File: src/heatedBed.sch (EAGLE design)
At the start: 10 parts

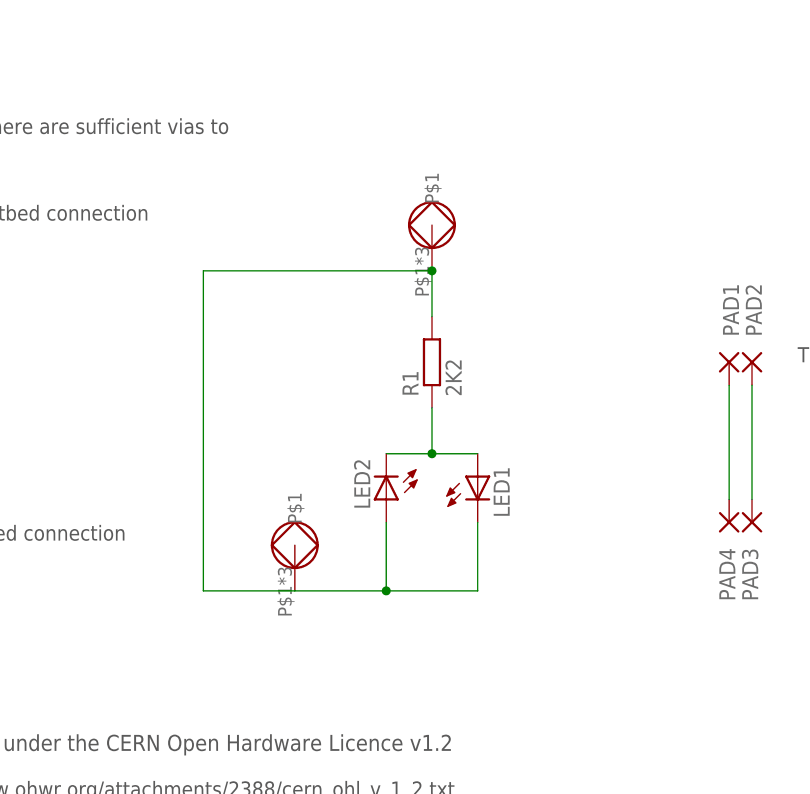
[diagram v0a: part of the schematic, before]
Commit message: Updated PCB for bottom mount LEDs
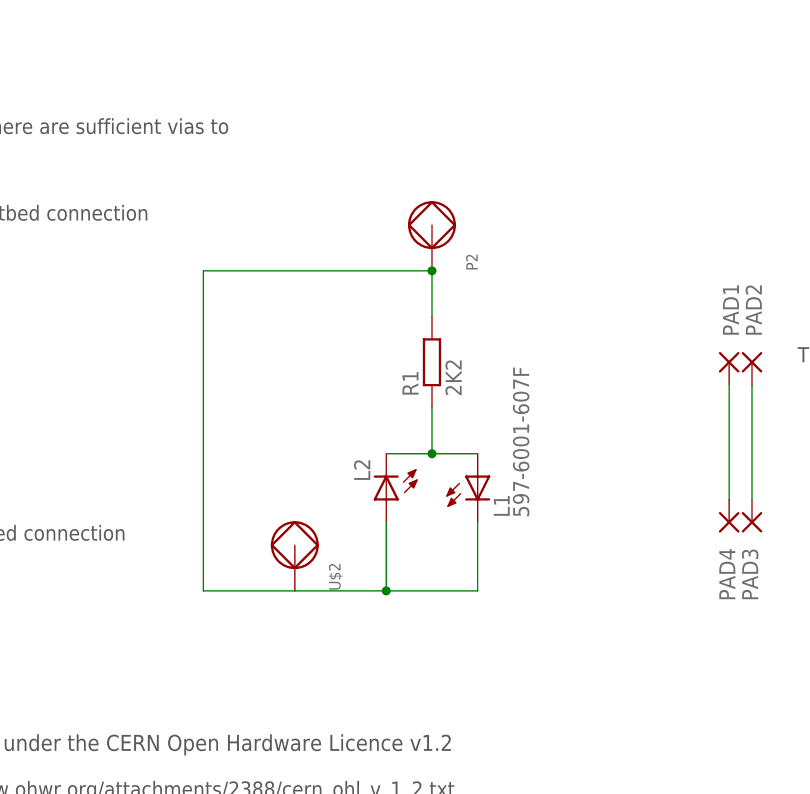
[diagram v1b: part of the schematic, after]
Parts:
- removed LED1, LED2: (no value), led:LEDCHIP-LED0805
- added L1: 597-6001-607F, led:LEDCHIPLED_1206_REV
- added L2: (no value), led:LEDCHIPLED_1206_REV
- renumbered U$3 to P2
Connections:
- removed net N$1: LED1.C, LED2.A, P2.P$1, R1.2, U$2.P$1
- new net P1: L1.C, L2.A, P2.P$1, R1.2, U$2.P$1
- net N$4: now also L1.A, L2.C; no longer LED1.A, LED2.C
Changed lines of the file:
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@@
 <part name="FRAME1" library="frames" deviceset="DINA4_L" device=""/>
 <part name="R1" library="rcl" deviceset="R-EU_" device="R0805" value="2K2"/>
-<part name="LED1" library="led" deviceset="LED" device="CHIP-LED0805"/>
-<part name="LED2" library="led" deviceset="LED" device="CHIP-LED0805"/>
+<part name="L1" library="led" deviceset="LED" device="CHIPLED_1206_REV" value="597-6001-607F"/>
+<part name="L2" library="led" deviceset="LED" device="CHIPLED_1206_REV"/>
 <part name="U$2" library="fmc" deviceset="LONG_PAD" device=""/>
-<part name="U$3" library="fmc" deviceset="LONG_PAD" device=""/>
+<part name="P2" library="fmc" deviceset="LONG_PAD" device=""/>
 <part name="PAD1" library="wirepad" deviceset="SMD5" device=""/>
 <part name="PAD2" library="wirepad" deviceset="SMD5" device=""/>
@@
 <instance part="FRAME1" gate="G$2" x="162.56" y="0"/>
 <instance part="R1" gate="G$1" x="73.66" y="58.42" rot="R90"/>
-<instance part="LED1" gate="G$1" x="78.74" y="45.72"/>
-<instance part="LED2" gate="G$1" x="68.58" y="43.18" rot="R180"/>
+<instance part="L1" gate="G$1" x="78.74" y="45.72"/>
+<instance part="L2" gate="G$1" x="68.58" y="43.18" rot="R180"/>
 <instance part="U$2" gate="G$1" x="58.42" y="33.02"/>
-<instance part="U$3" gate="G$1" x="73.66" y="68.58"/>
+<instance part="P2" gate="G$1" x="73.66" y="68.58"/>
 <instance part="PAD1" gate="1" x="106.68" y="58.42" smashed="yes" rot="R270">
 <attribute name="NAME" x="105.9942" y="67.183" size="1.778" layer="95" rot="R270"/>
@@
 </busses>
 <nets>
-<net name="N$1" class="0">
+<net name="P1" class="0">
 <segment>
-<pinref part="U$3" gate="G$1" pin="P$1"/>
+<pinref part="P2" gate="G$1" pin="P$1"/>
 <pinref part="R1" gate="G$1" pin="2"/>
 <wire x1="73.66" y1="68.58" x2="73.66" y2="63.5" width="0.1524" layer="91"/>
@@
 <wire x1="48.26" y1="68.58" x2="48.26" y2="33.02" width="1.27" layer="91"/>
 <pinref part="U$2" gate="G$1" pin="P$1"/>
-<pinref part="LED2" gate="G$1" pin="A"/>
+<pinref part="L2" gate="G$1" pin="A"/>
 <wire x1="58.42" y1="33.02" x2="68.58" y2="33.02" width="0.1524" layer="91"/>
 <wire x1="68.58" y1="33.02" x2="68.58" y2="40.64" width="0.1524" layer="91"/>
-<pinref part="LED1" gate="G$1" pin="C"/>
+<pinref part="L1" gate="G$1" pin="C"/>
 <wire x1="78.74" y1="40.64" x2="78.74" y2="33.02" width="0.1524" layer="91"/>
 <wire x1="78.74" y1="33.02" x2="68.58" y2="33.02" width="0.1524" layer="91"/>
@@
 <net name="N$4" class="0">
 <segment>
-<pinref part="LED2" gate="G$1" pin="C"/>
+<pinref part="L2" gate="G$1" pin="C"/>
 <pinref part="R1" gate="G$1" pin="1"/>
 <wire x1="68.58" y1="48.26" x2="73.66" y2="48.26" width="0.1524" layer="91"/>
 <wire x1="73.66" y1="48.26" x2="73.66" y2="53.34" width="0.1524" layer="91"/>
-<pinref part="LED1" gate="G$1" pin="A"/>
+<pinref part="L1" gate="G$1" pin="A"/>
 <wire x1="78.74" y1="48.26" x2="73.66" y2="48.26" width="0.1524" layer="91"/>
 <junction x="73.66" y="48.26"/>

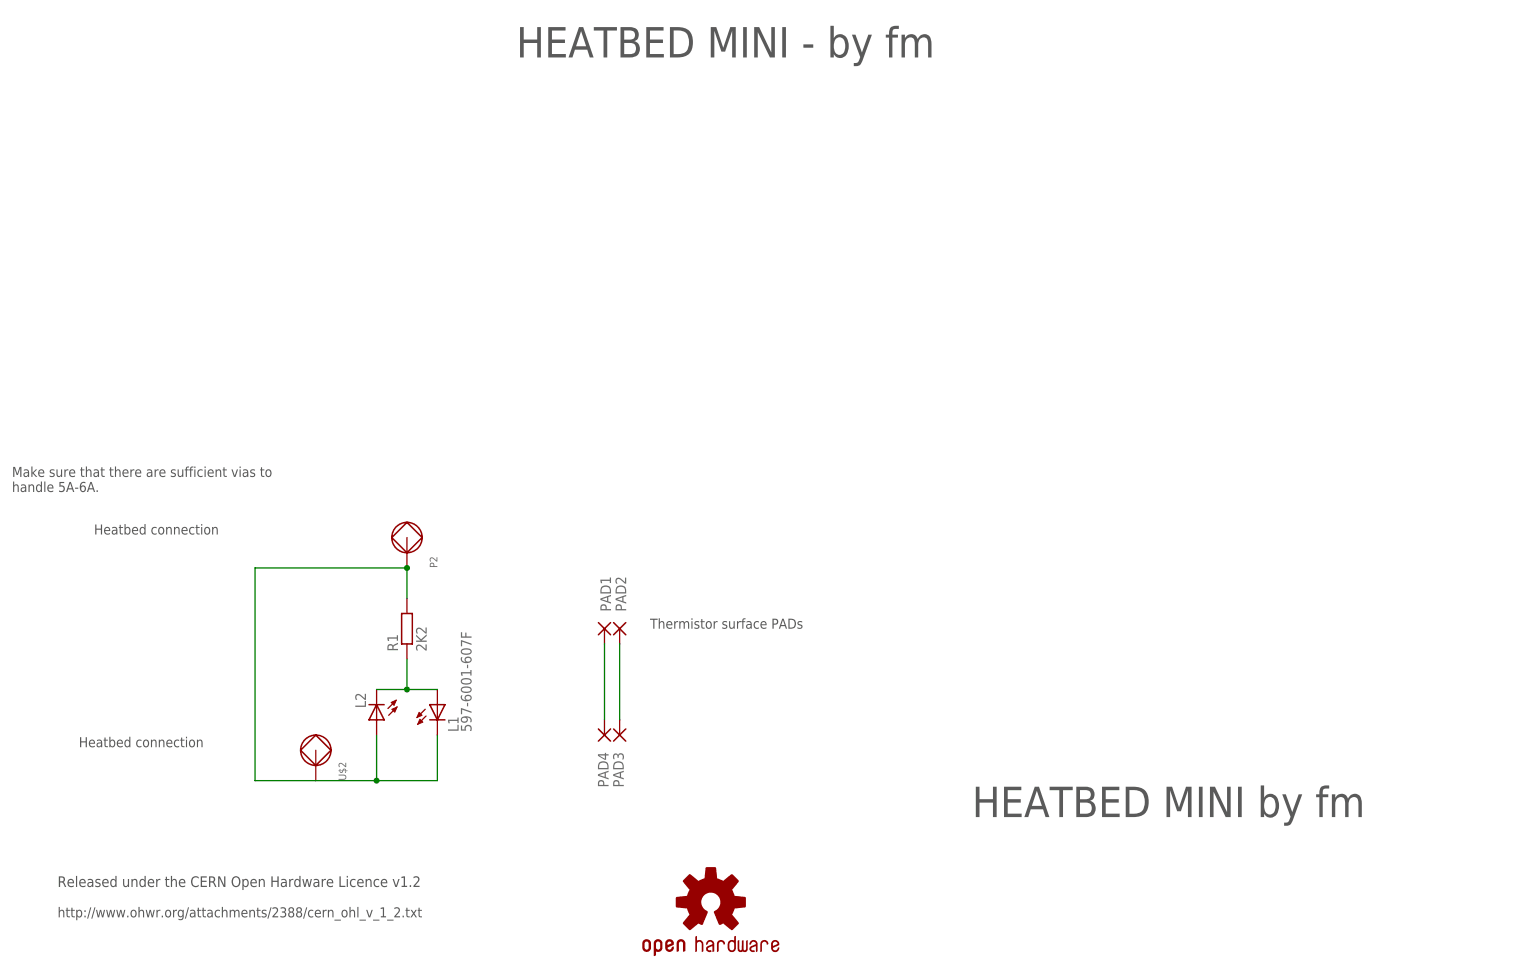
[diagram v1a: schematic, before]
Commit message: Updated schematic with boar revision and arrangement.
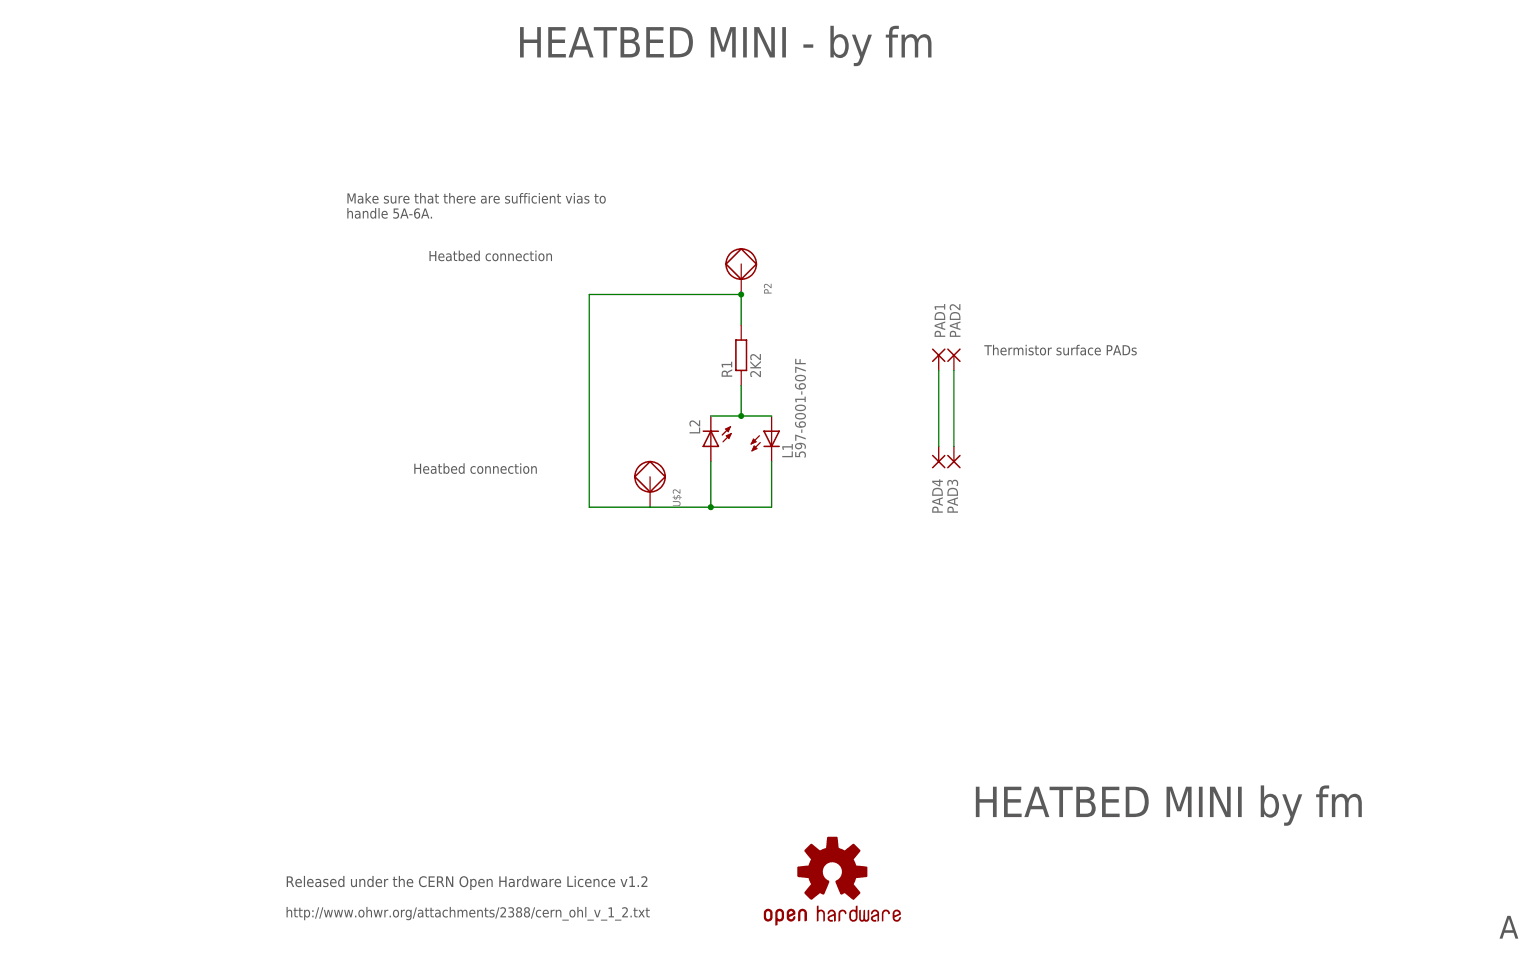
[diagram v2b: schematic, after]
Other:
- note added: "A"
- moved on the sheet: L1, L2, P2, PAD1, PAD2, PAD3, PAD4, R1, U$2
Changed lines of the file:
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@@
 <sheet>
 <plain>
-<text x="15.24" y="15.24" size="1.778" layer="97">Released under the CERN Open Hardware Licence v1.2 </text>
+<text x="53.34" y="15.24" size="1.778" layer="97">Released under the CERN Open Hardware Licence v1.2 </text>
 <text x="168.148" y="26.924" size="5.08" layer="97">HEATBED MINI by fm</text>
-<text x="21.336" y="74.168" size="1.6764" layer="97">Heatbed connection</text>
-<text x="18.796" y="38.608" size="1.6764" layer="97">Heatbed connection</text>
-<text x="7.62" y="81.28" size="1.6764" layer="97">Make sure that there are sufficient vias to
+<text x="77.216" y="119.888" size="1.6764" layer="97">Heatbed connection</text>
+<text x="74.676" y="84.328" size="1.6764" layer="97">Heatbed connection</text>
+<text x="63.5" y="127" size="1.6764" layer="97">Make sure that there are sufficient vias to
 handle 5A-6A.</text>
-<text x="114.3" y="58.42" size="1.6764" layer="97">Thermistor surface PADs</text>
-<text x="15.24" y="10.16" size="1.6764" layer="97">http://www.ohwr.org/attachments/2388/cern_ohl_v_1_2.txt</text>
+<text x="170.18" y="104.14" size="1.6764" layer="97">Thermistor surface PADs</text>
+<text x="53.34" y="10.16" size="1.6764" layer="97">http://www.ohwr.org/attachments/2388/cern_ohl_v_1_2.txt</text>
 <text x="91.948" y="153.924" size="5.08" layer="97">HEATBED MINI - by fm</text>
+<text x="256.286" y="6.604" size="3.81" layer="97">A</text>
 </plain>
 <instances>
 <instance part="FRAME1" gate="G$1" x="0" y="0"/>
 <instance part="FRAME1" gate="G$2" x="162.56" y="0"/>
-<instance part="R1" gate="G$1" x="73.66" y="58.42" rot="R90"/>
-<instance part="L1" gate="G$1" x="78.74" y="45.72"/>
-<instance part="L2" gate="G$1" x="68.58" y="43.18" rot="R180"/>
-<instance part="U$2" gate="G$1" x="58.42" y="33.02"/>
-<instance part="P2" gate="G$1" x="73.66" y="68.58"/>
-<instance part="PAD1" gate="1" x="106.68" y="58.42" smashed="yes" rot="R270">
-<attribute name="NAME" x="105.9942" y="67.183" size="1.778" layer="95" rot="R270"/>
-<attribute name="VALUE" x="103.378" y="59.563" size="1.778" layer="96" rot="R270"/>
+<instance part="R1" gate="G$1" x="129.54" y="104.14" rot="R90"/>
+<instance part="L1" gate="G$1" x="134.62" y="91.44"/>
+<instance part="L2" gate="G$1" x="124.46" y="88.9" rot="R180"/>
+<instance part="U$2" gate="G$1" x="114.3" y="78.74"/>
+<instance part="P2" gate="G$1" x="129.54" y="114.3"/>
+<instance part="PAD1" gate="1" x="162.56" y="104.14" smashed="yes" rot="R270">
+<attribute name="NAME" x="161.8742" y="112.903" size="1.778" layer="95" rot="R270"/>
+<attribute name="VALUE" x="159.258" y="105.283" size="1.778" layer="96" rot="R270"/>
 </instance>
-<instance part="PAD2" gate="1" x="109.22" y="58.42" smashed="yes" rot="R270">
-<attribute name="NAME" x="108.5342" y="67.183" size="1.778" layer="95" rot="R270"/>
-<attribute name="VALUE" x="105.918" y="59.563" size="1.778" layer="96" rot="R270"/>
+<instance part="PAD2" gate="1" x="165.1" y="104.14" smashed="yes" rot="R270">
+<attribute name="NAME" x="164.4142" y="112.903" size="1.778" layer="95" rot="R270"/>
+<attribute name="VALUE" x="161.798" y="105.283" size="1.778" layer="96" rot="R270"/>
 </instance>
-<instance part="PAD3" gate="1" x="109.22" y="40.64" smashed="yes" rot="R90">
-<attribute name="NAME" x="109.9058" y="31.877" size="1.778" layer="95" rot="R90"/>
-<attribute name="VALUE" x="112.522" y="39.497" size="1.778" layer="96" rot="R90"/>
+<instance part="PAD3" gate="1" x="165.1" y="86.36" smashed="yes" rot="R90">
+<attribute name="NAME" x="165.7858" y="77.597" size="1.778" layer="95" rot="R90"/>
+<attribute name="VALUE" x="168.402" y="85.217" size="1.778" layer="96" rot="R90"/>
 </instance>
-<instance part="PAD4" gate="1" x="106.68" y="40.64" smashed="yes" rot="R90">
-<attribute name="NAME" x="107.3658" y="31.877" size="1.778" layer="95" rot="R90"/>
-<attribute name="VALUE" x="109.982" y="39.497" size="1.778" layer="96" rot="R90"/>
+<instance part="PAD4" gate="1" x="162.56" y="86.36" smashed="yes" rot="R90">
+<attribute name="NAME" x="163.2458" y="77.597" size="1.778" layer="95" rot="R90"/>
+<attribute name="VALUE" x="165.862" y="85.217" size="1.778" layer="96" rot="R90"/>
 </instance>
-<instance part="U$5" gate="G$1" x="124.46" y="12.7"/>
+<instance part="U$5" gate="G$1" x="144.78" y="17.78"/>
 </instances>
 <busses>
@@
 <pinref part="P2" gate="G$1" pin="P$1"/>
 <pinref part="R1" gate="G$1" pin="2"/>
-<wire x1="73.66" y1="68.58" x2="73.66" y2="63.5" width="0.1524" layer="91"/>
-<wire x1="73.66" y1="68.58" x2="48.26" y2="68.58" width="1.27" layer="91"/>
-<wire x1="48.26" y1="68.58" x2="48.26" y2="33.02" width="1.27" layer="91"/>
+<wire x1="129.54" y1="114.3" x2="129.54" y2="109.22" width="0.1524" layer="91"/>
+<wire x1="129.54" y1="114.3" x2="104.14" y2="114.3" width="1.27" layer="91"/>
+<wire x1="104.14" y1="114.3" x2="104.14" y2="78.74" width="1.27" layer="91"/>
 <pinref part="U$2" gate="G$1" pin="P$1"/>
 <pinref part="L2" gate="G$1" pin="A"/>
-<wire x1="58.42" y1="33.02" x2="68.58" y2="33.02" width="0.1524" layer="91"/>
-<wire x1="68.58" y1="33.02" x2="68.58" y2="40.64" width="0.1524" layer="91"/>
+<wire x1="114.3" y1="78.74" x2="124.46" y2="78.74" width="0.1524" layer="91"/>
+<wire x1="124.46" y1="78.74" x2="124.46" y2="86.36" width="0.1524" layer="91"/>
 <pinref part="L1" gate="G$1" pin="C"/>
-<wire x1="78.74" y1="40.64" x2="78.74" y2="33.02" width="0.1524" layer="91"/>
-<wire x1="78.74" y1="33.02" x2="68.58" y2="33.02" width="0.1524" layer="91"/>
-<junction x="68.58" y="33.02"/>
-<wire x1="48.26" y1="33.02" x2="58.42" y2="33.02" width="1.27" layer="91"/>
-<junction x="73.66" y="68.58"/>
+<wire x1="134.62" y1="86.36" x2="134.62" y2="78.74" width="0.1524" layer="91"/>
+<wire x1="134.62" y1="78.74" x2="124.46" y2="78.74" width="0.1524" layer="91"/>
+<junction x="124.46" y="78.74"/>
+<wire x1="104.14" y1="78.74" x2="114.3" y2="78.74" width="1.27" layer="91"/>
+<junction x="129.54" y="114.3"/>
 </segment>
 </net>
@@
 <pinref part="L2" gate="G$1" pin="C"/>
 <pinref part="R1" gate="G$1" pin="1"/>
-<wire x1="68.58" y1="48.26" x2="73.66" y2="48.26" width="0.1524" layer="91"/>
-<wire x1="73.66" y1="48.26" x2="73.66" y2="53.34" width="0.1524" layer="91"/>
+<wire x1="124.46" y1="93.98" x2="129.54" y2="93.98" width="0.1524" layer="91"/>
+<wire x1="129.54" y1="93.98" x2="129.54" y2="99.06" width="0.1524" layer="91"/>
 <pinref part="L1" gate="G$1" pin="A"/>
-<wire x1="78.74" y1="48.26" x2="73.66" y2="48.26" width="0.1524" layer="91"/>
-<junction x="73.66" y="48.26"/>
+<wire x1="134.62" y1="93.98" x2="129.54" y2="93.98" width="0.1524" layer="91"/>
+<junction x="129.54" y="93.98"/>
 </segment>
 </net>
@@
 <segment>
 <pinref part="PAD1" gate="1" pin="P"/>
-<wire x1="106.68" y1="55.88" x2="106.68" y2="43.18" width="0.1524" layer="91"/>
+<wire x1="162.56" y1="101.6" x2="162.56" y2="88.9" width="0.1524" layer="91"/>
 <pinref part="PAD4" gate="1" pin="P"/>
 </segment>
@@
 <segment>
 <pinref part="PAD2" gate="1" pin="P"/>
-<wire x1="109.22" y1="55.88" x2="109.22" y2="43.18" width="0.1524" layer="91"/>
+<wire x1="165.1" y1="101.6" x2="165.1" y2="88.9" width="0.1524" layer="91"/>
 <pinref part="PAD3" gate="1" pin="P"/>
 </segment>

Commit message: Prepare Rev B release.
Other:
- note added: "B"
- note added: "RevA - 110W - track width = 1.41 aprox RevB - 69W - track width = 0.82 aprox"
- note removed: "A"
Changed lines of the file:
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@@
 <?xml version="1.0" encoding="utf-8"?>
 <!DOCTYPE eagle SYSTEM "eagle.dtd">
-<eagle version="7.0.0">
+<eagle version="7.4.0">
 <drawing>
 <settings>
@@
 <text x="53.34" y="10.16" size="1.6764" layer="97">http://www.ohwr.org/attachments/2388/cern_ohl_v_1_2.txt</text>
 <text x="91.948" y="153.924" size="5.08" layer="97">HEATBED MINI - by fm</text>
-<text x="256.286" y="6.604" size="3.81" layer="97">A</text>
+<text x="256.286" y="6.604" size="3.81" layer="97">B</text>
+<text x="66.04" y="60.96" size="1.778" layer="97" ratio="15">RevA - 110W - track width = 1.41 aprox
+RevB - 69W - track width = 0.82 aprox</text>
+<wire x1="104.14" y1="78.74" x2="91.44" y2="68.58" width="0.6096" layer="98"/>
 </plain>
 <instances>

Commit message: Prepared for Rev B.
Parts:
- added R2: NTCS0805E3104FXT, rcl:R-EU_R0805
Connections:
- net N$3: now also R2.2
- net N$5: now also R2.1
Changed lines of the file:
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@@
 <part name="PAD4" library="wirepad" deviceset="SMD5" device=""/>
 <part name="U$5" library="SAVLibSAV MK-I" deviceset="SPARKFUN_OSHW-LOGO" device="L"/>
+<part name="R2" library="rcl" deviceset="R-EU_" device="R0805" value="NTCS0805E3104FXT"/>
 </parts>
 <sheets>
@@
 </instance>
 <instance part="U$5" gate="G$1" x="144.78" y="17.78"/>
+<instance part="R2" gate="G$1" x="162.56" y="121.92" smashed="yes" rot="R180">
+<attribute name="NAME" x="166.37" y="120.4214" size="1.778" layer="95" rot="R180"/>
+<attribute name="VALUE" x="178.816" y="125.984" size="1.778" layer="96" rot="R180"/>
+</instance>
 </instances>
 <busses>
@@
 <wire x1="162.56" y1="101.6" x2="162.56" y2="88.9" width="0.1524" layer="91"/>
 <pinref part="PAD4" gate="1" pin="P"/>
+<pinref part="R2" gate="G$1" pin="2"/>
+<wire x1="157.48" y1="121.92" x2="152.4" y2="121.92" width="0.1524" layer="91"/>
+<wire x1="152.4" y1="121.92" x2="152.4" y2="101.6" width="0.1524" layer="91"/>
+<wire x1="152.4" y1="101.6" x2="162.56" y2="101.6" width="0.1524" layer="91"/>
+<junction x="162.56" y="101.6"/>
 </segment>
 </net>
@@
 <wire x1="165.1" y1="101.6" x2="165.1" y2="88.9" width="0.1524" layer="91"/>
 <pinref part="PAD3" gate="1" pin="P"/>
+<wire x1="165.1" y1="101.6" x2="175.26" y2="101.6" width="0.1524" layer="91"/>
+<wire x1="175.26" y1="101.6" x2="175.26" y2="121.92" width="0.1524" layer="91"/>
+<junction x="165.1" y="101.6"/>
+<pinref part="R2" gate="G$1" pin="1"/>
+<wire x1="175.26" y1="121.92" x2="167.64" y2="121.92" width="0.1524" layer="91"/>
 </segment>
 </net>
